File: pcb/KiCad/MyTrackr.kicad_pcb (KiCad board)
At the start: 2 copper layers, 50 x 50 mm, 41 parts, among them CN1 GPS_ANTENNA, CON1 MICRO_SD, J1 REGULATOR_3V3, J2 CONN_ICSP, J3 CONN_SERIAL, J4 CONN_BAT, P1 CONN_OLED, Q1 Q_PMOS_GSD, SW1 BTN_RESET, SW2 BTN_BACK, SW3 BTN_PREV, SW4 BTN_NEXT, SW5 BTN_SEL, U1 ATmega328P-AU, U2 GPS-NEO-6M, U3 24AA32

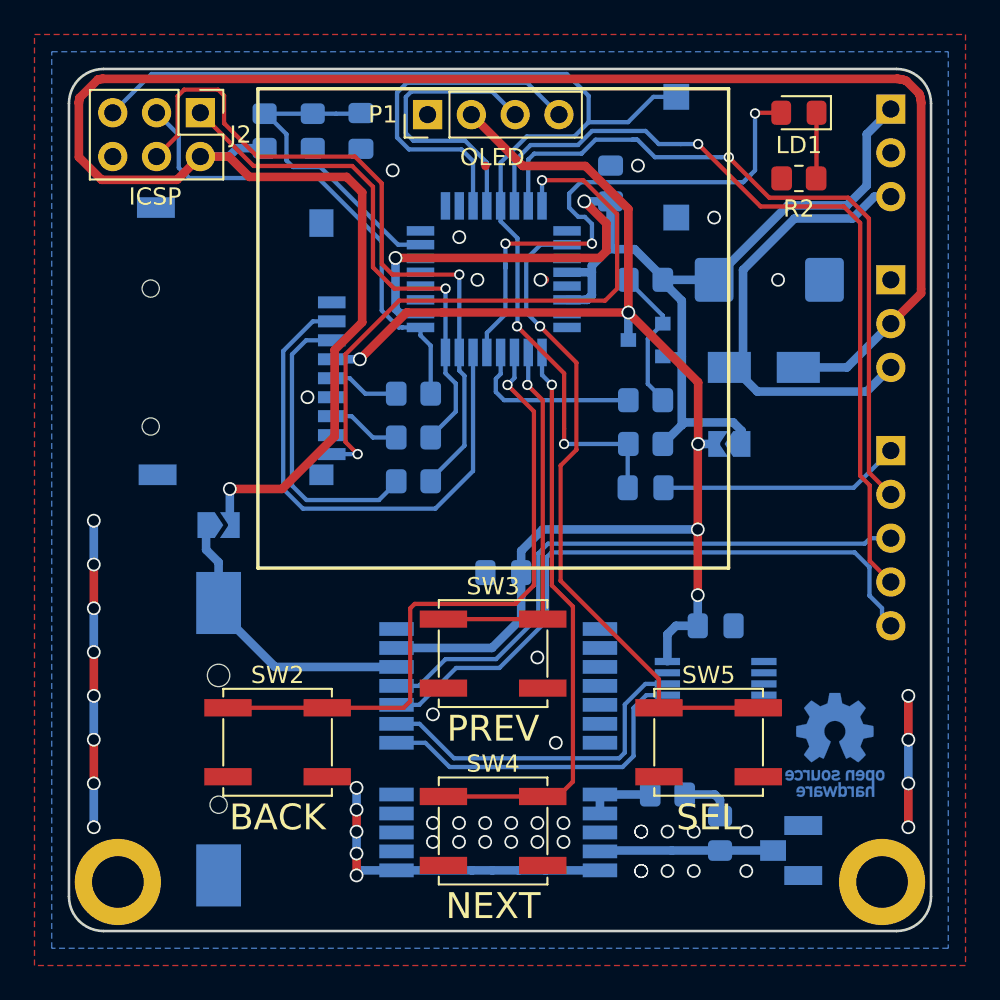
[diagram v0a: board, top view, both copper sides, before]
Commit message: Add i2c pull-ups
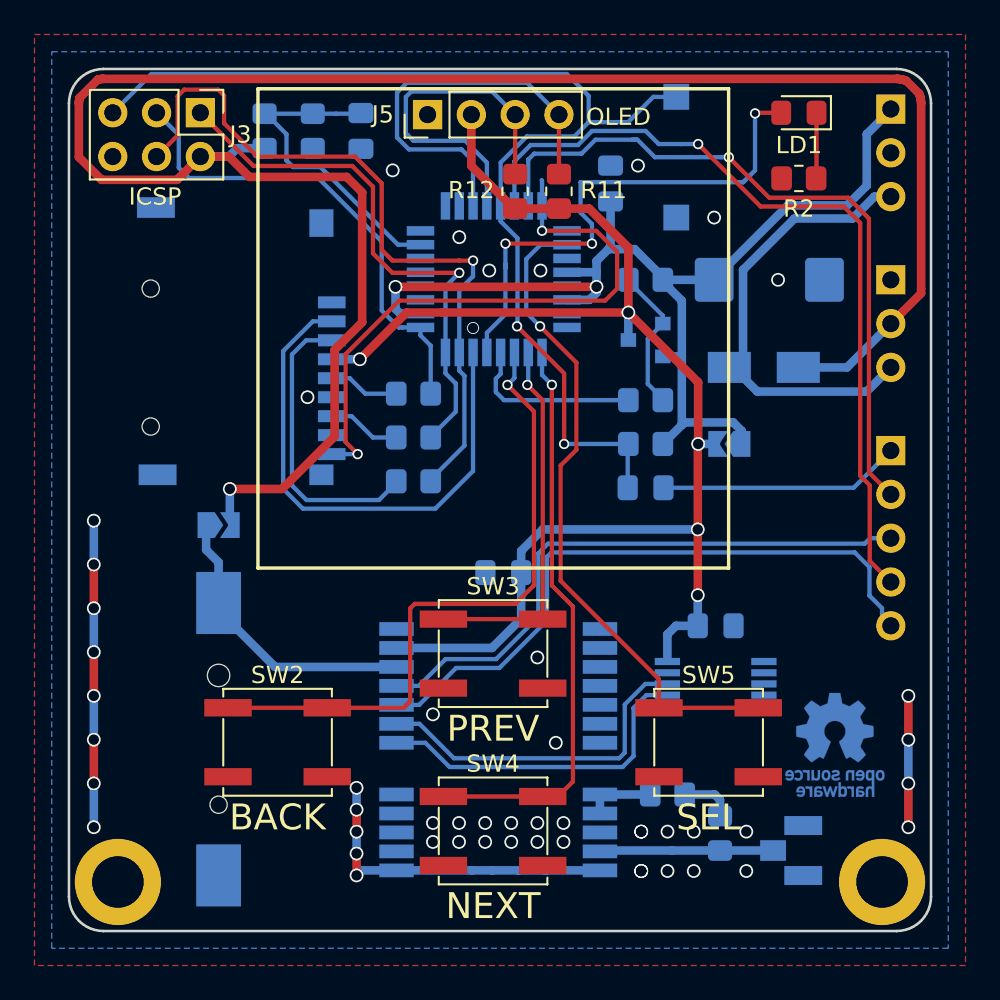
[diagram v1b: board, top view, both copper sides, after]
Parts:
- added R11: 3.3k, Resistor_SMD:R_0805_2012Metric_Pad1.20x1.40mm_HandSolder, F.Cu at (118.4, 57.1)
- added R12: 3.3k, Resistor_SMD:R_0805_2012Metric_Pad1.20x1.40mm_HandSolder, F.Cu at (115.9, 57.1)
- renumbered J4 to J2, J2 to J3, J3 to J4, P1 to J5
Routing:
- net +3V3: track 70.1 -> 62.9 mm
- net /sda: track 20.6 -> 23.6 mm
- net /scl: track 17.0 -> 20.1 mm
- net VPP: track 84.6 -> 87.2 mm
- net /miso: track 30.2 -> 31.9 mm
- net /mosi: track 41.5 -> 42.7 mm
- net /CARD_DETECT: track 35.9 -> 34.8 mm
- net /act_led: track 32.1 -> 31.3 mm
- net GND: track 49.2 -> 48.8 mm, vias 51 -> 52

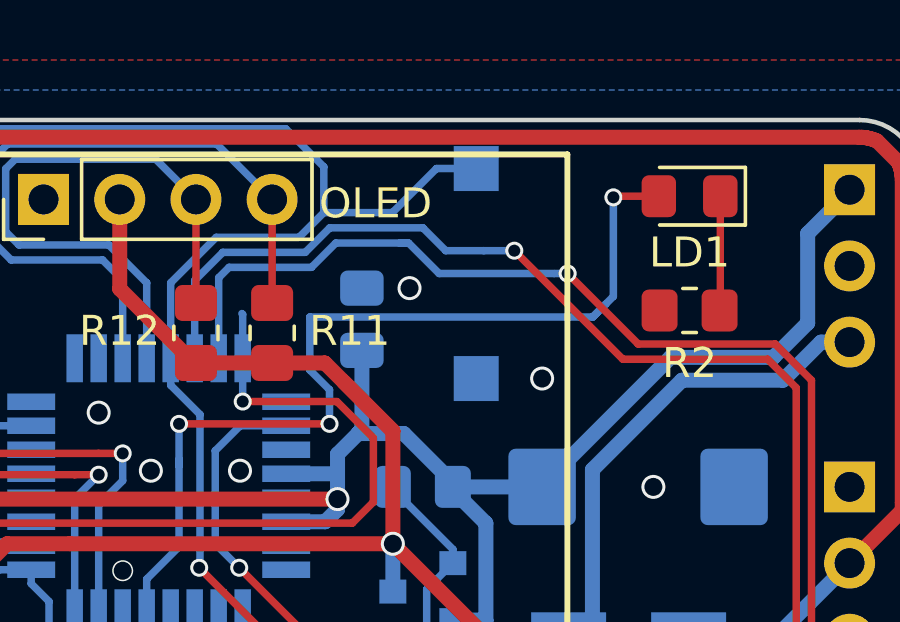
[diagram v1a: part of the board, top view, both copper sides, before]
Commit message: Minor fixes after PCB production
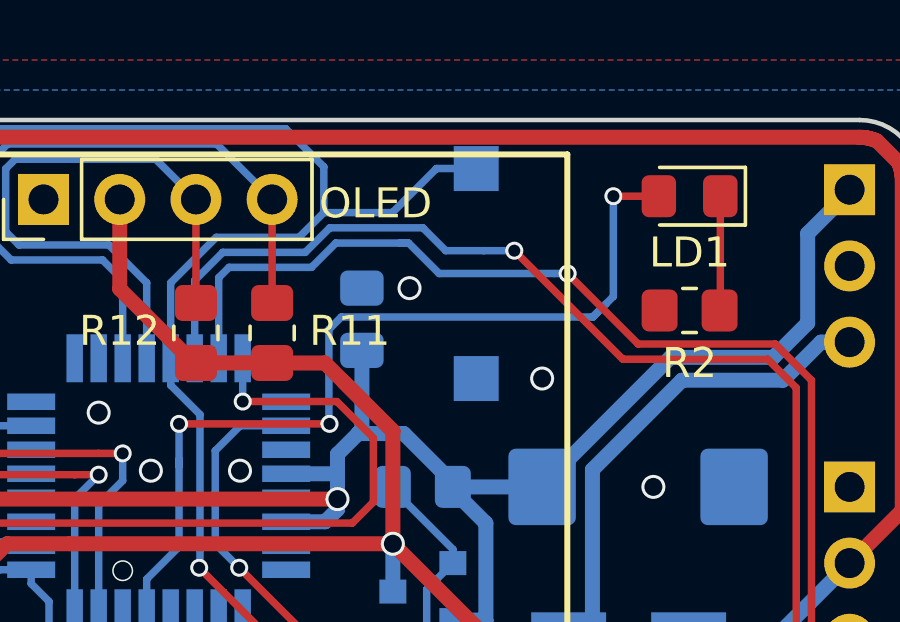
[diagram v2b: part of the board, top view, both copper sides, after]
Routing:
- net /CARD_DETECT: track 34.8 -> 33.3 mm
- net /act_led: track 31.3 -> 30.1 mm
